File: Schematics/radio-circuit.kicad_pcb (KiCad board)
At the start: 4 copper layers, 59 x 29.5 mm, 36 parts, among them J2 STDC14, J3 0, J4 USB_A, U1 USBLC6-2SC6, U2 LD39015M33R, U3 STM32F042F6Px, U4 Si4705-D60-GM, Y1 SG-3030CM

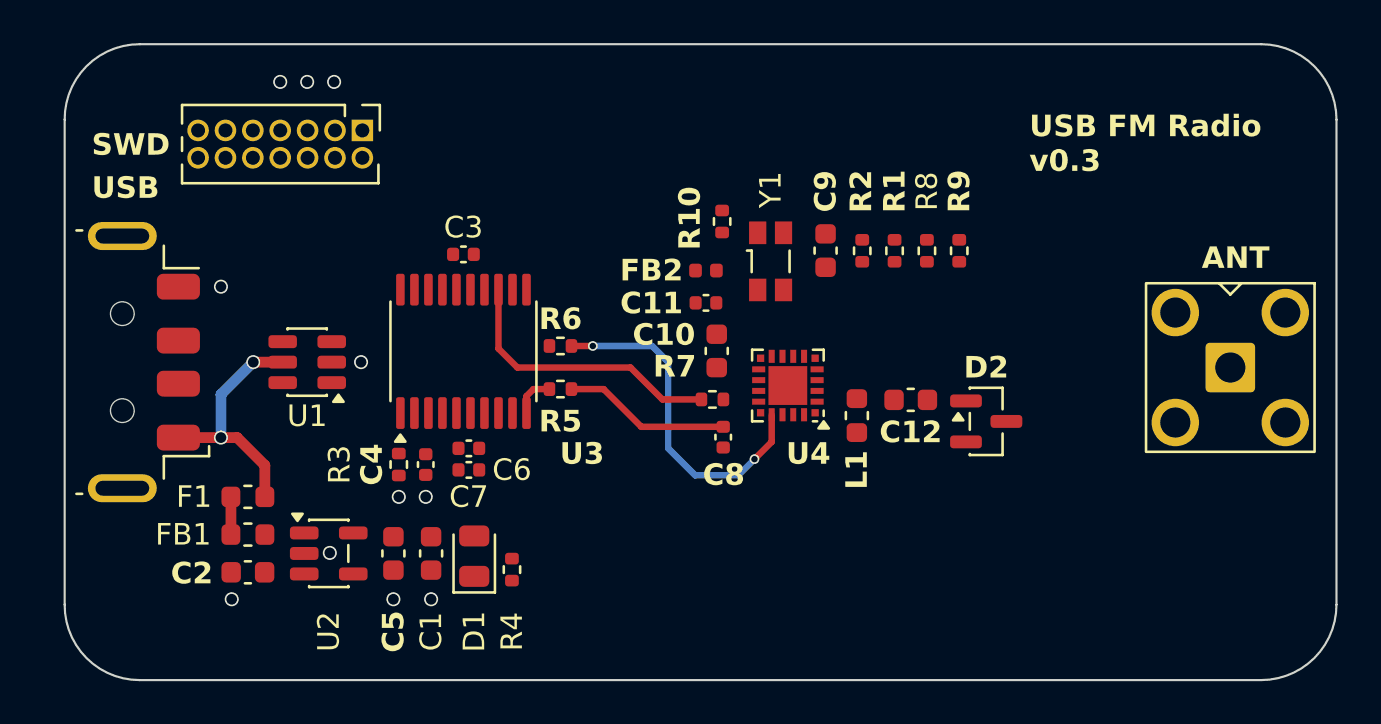
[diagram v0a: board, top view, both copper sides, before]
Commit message: Finished component placement
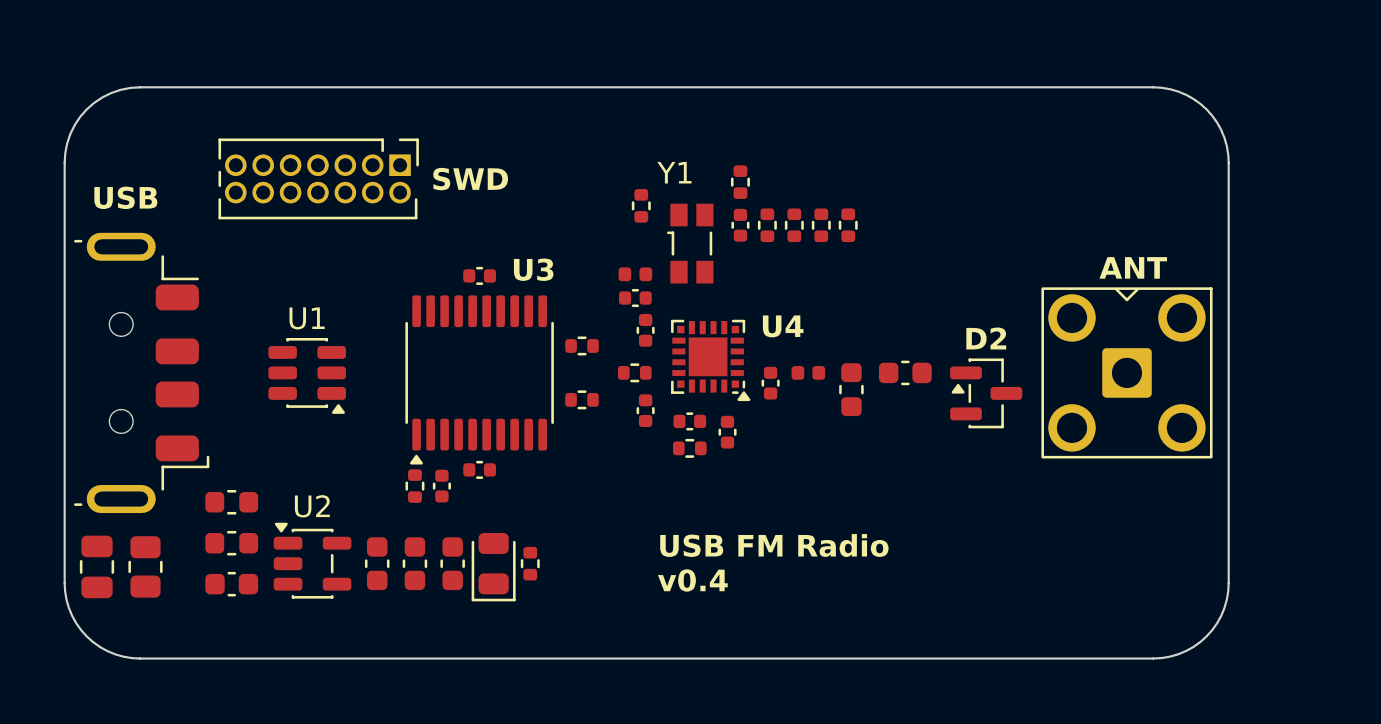
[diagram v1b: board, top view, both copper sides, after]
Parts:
- removed J4: USB_A, Local:USB_A_Molex_48037-2200_Horizontal
- added C13: 33p, Capacitor_SMD:C_0402_1005Metric, F.Cu at (192.8, 128.0)
- added C14: 6p, Capacitor_SMD:C_0402_1005Metric, F.Cu at (194.8, 125.7)
- added C15: 33p, Capacitor_SMD:C_0402_1005Metric, F.Cu at (191.0, 127.5)
- added C16: 1n, Capacitor_SMD:C_0603_1608Metric, F.Cu at (201.0, 125.2)
- added FB3: 75@100MHz, Inductor_SMD:L_0402_1005Metric, F.Cu at (196.5, 125.2)
- added J1: USB_A, Local:USB_A_Molex_48037-2200_Horizontal, F.Cu at (156.2, 125.2)
- added R11: 22, Resistor_SMD:R_0402_1005Metric, F.Cu at (193.3, 116.4)
- added R12: 10k, Resistor_SMD:R_0402_1005Metric, F.Cu at (188.8, 117.5)
- added R13: 330, Resistor_SMD:R_0402_1005Metric, F.Cu at (191.0, 128.8)
- C1: value 4.7u -> 100n; footprint Capacitor_SMD:C_0603_1608Metric -> Capacitor_SMD:C_0805_2012Metric
- C10: value 22n -> 100n; footprint Capacitor_SMD:C_0603_1608Metric -> Capacitor_SMD:C_0402_1005Metric
- C11: value 100n -> 22n
- C12: value 1n -> 100n; footprint Capacitor_SMD:C_0603_1608Metric -> Capacitor_SMD:C_0402_1005Metric
- C3: value 100n -> 4.7u; footprint Capacitor_SMD:C_0402_1005Metric -> Capacitor_SMD:C_0603_1608Metric
- C5: value 4.7u -> 100n; footprint Capacitor_SMD:C_0603_1608Metric -> Capacitor_SMD:C_0402_1005Metric
- C6: value 10n -> 4.7u; footprint Capacitor_SMD:C_0402_1005Metric -> Capacitor_SMD:C_0603_1608Metric
- C7: value 1u -> 10n
- C8: value 2.2p -> 1u; footprint Capacitor_SMD:C_0402_1005Metric -> Capacitor_SMD:C_0603_1608Metric
- C9: value 47n -> 2.2p; footprint Capacitor_SMD:C_0603_1608Metric -> Capacitor_SMD:C_0402_1005Metric
- R1: value 4k7 -> 1M; footprint Resistor_SMD:R_0402_1005Metric -> Resistor_SMD:R_0805_2012Metric
- R3: value 10k -> 4k7
- R4: value 1k5 -> 10k
- R5: value 2k -> 1k5
- R7: value 604 -> 2k
- R8: value 10k -> 604
- moved R1 37.7 mm to (165.8, 134.2), turned to 90 degrees
- moved R3 21.4 mm to (195.8, 118.4)
- moved C3 18.7 mm to (169.8, 135.1), turned to 180 degrees
- moved C1 15.5 mm to (163.5, 134.2), turned to 90 degrees
- moved R8 14.7 mm to (188.4, 125.2), turned to 0 degrees
- moved C8 13.9 mm to (180.0, 134.1)
- moved C12 12.7 mm to (188.9, 123.3), turned to -90 degrees
- moved C9 11.2 mm to (188.9, 127.0)
- moved R5 8.22 mm to (183.6, 134.1), turned to 90 degrees
- moved C7 8.02 mm to (181.2, 120.8)
- moved C2 7.76 mm to (178.2, 134.1), turned to -90 degrees
- moved R7 6.54 mm to (186.0, 124.0)
- moved R9 6.51 mm to (197.1, 118.4)
- moved C6 6.08 mm to (176.5, 134.1), turned to -90 degrees
- moved R4 5.94 mm to (178.2, 130.5), turned to -90 degrees
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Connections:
- C1 pad 1: +3.3V -> GND
- C1 pad 2: GND -> /SHD
- C10 pad 1: V_{RADIO} -> V_{OSC}
- C12 pad 1: /ANT -> V_{RADIO}
- C12 pad 2: /FMI -> GND
- C2 pad 1: V_{FILT} -> +3.3V
- C3 pad 1: +3.3V -> V_{LDO}
- C4 pad 1: NRST -> +3.3V
- C5 pad 1: +3.3V -> NRST
- C8 pad 1: I2S_WS -> +3.3V
- C9 pad 1: +3.3V -> I2S_WS
- FB1 pad 2: V_{FILT} -> V_{LDO}
- L1 pad 2: /FMI -> /TUNE
- R1 pad 1: +3.3V -> GND
- R1 pad 2: I2C_SCL -> /SHD
- R10 pad 1: OSC_EN -> GND
- R10 pad 2: GND -> ~{RD_RST}
- R2 pad 2: I2C_SDA -> I2C_SCL
- R3 pad 1: /BOOT -> +3.3V
- R3 pad 2: GND -> I2C_SDA
- R4 pad 1: /PWR_LED_K -> /BOOT
- R5 pad 1: /PA4 -> /PWR_LED_K
- R5 pad 2: I2S_WS -> GND
- R6 pad 1: /PA5 -> /PA4
- R6 pad 2: I2S_CK -> I2S_WS
- R7 pad 1: I2S_SD -> /PA5
- R7 pad 2: /DOUT -> I2S_CK
- R8 pad 1: GND -> I2S_SD
- R8 pad 2: / ~{SEN} -> /DOUT
- R9 pad 2: ~{RD_RST} -> / ~{SEN}
- U2 pad 1: V_{FILT} -> V_{LDO}
- U2 pad 3: V_{FILT} -> V_{LDO}
- U4 pad 18: ~{RD_IRQ} -> /GPO2
- U4 pad 19: unconnected-(U4-GPO1-Pad19) -> /GPO1
- Y1 pad 4: +3.3V -> V_{OSC}
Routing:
- net I2S_CK: track 16.0 -> 0.00 mm, vias 2 -> 0
- net I2S_SD: track 13.1 -> 0.00 mm
- net V_{BUS}: track 11.5 -> 0.00 mm, vias 2 -> 0
- net I2S_WS: track 7.76 -> 0.00 mm
- net /PA4: track 2.00 -> 0.00 mm
- net /FUSE: track 1.75 -> 0.00 mm
- net GND: vias 10 -> 0
- net +3.3V: vias 1 -> 0
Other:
- board size 59 x 29.5 mm -> 54 x 26.5 mm
- board text added: "USB FM Radio v0.4"
- board text removed: "USB FM Radio v0.3"

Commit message: Finished traces and layers
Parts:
- moved C5 14.4 mm to (170.7, 119.1), turned to 180 degrees
- moved R3 1.35 mm to (194.5, 118.4)
- moved R2 1.10 mm to (195.7, 118.4)
- moved R11 0.76 mm to (194.0, 116.8), turned to 0 degrees
- moved C1 0.50 mm to (164.0, 134.2)
- moved R1 0.50 mm to (166.2, 134.2)
- moved C11 0.32 mm to (188.2, 122.0)
- moved C12 0.30 mm to (188.8, 123.5)
- moved FB2 0.26 mm to (188.2, 120.8)
- moved R10 0.25 mm to (198.1, 118.4)
- moved C9 0.20 mm to (188.8, 127.0)
- moved R9 0.20 mm to (196.9, 118.4)
- moved R8 0.20 mm to (188.2, 125.2)
- moved C4 0.16 mm to (181.4, 129.8)
- moved R12 0.11 mm to (188.7, 117.4)
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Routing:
- net +3.3V: track 0.00 -> 56.6 mm, vias 0 -> 10
- net GND: track 0.00 -> 45.1 mm, vias 0 -> 97
- net ~{RD_RST}: track 0.00 -> 27.1 mm, vias 0 -> 2
- net I2C_SDA: track 0.00 -> 25.0 mm, vias 0 -> 2
- net I2C_SCL: track 0.00 -> 24.3 mm, vias 0 -> 2
- net NRST: track 0.00 -> 17.3 mm, vias 0 -> 2
- net /SHD: track 0.00 -> 15.7 mm
- net V_{BUS}: track 0.00 -> 10.5 mm, vias 0 -> 2
- net OSC_EN: track 0.00 -> 9.77 mm
- net /ANT: track 0.00 -> 9.55 mm
- net ~{RD_IRQ}: track 0.00 -> 8.74 mm
- net USB_D-: track 0.00 -> 8.63 mm
- net USB_D+: track 0.00 -> 7.82 mm
- net / ~{SEN}: track 0.00 -> 7.20 mm
- net I2S_SD: track 0.00 -> 7.16 mm
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- added copper zone on F.Cu, net +3.3V
- added copper zone on F.Cu, net /SHD
- added copper zone on B.Cu, net GND
- added copper zone on F.Cu, net GND
- added copper zone on In1.Cu, net GND
- added copper zone on In2.Cu, net GND

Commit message: Fixed via placement for QFN and re-routed STM32 NRST
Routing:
- net NRST: track 17.3 -> 21.4 mm
- net GND: track 45.1 -> 46.3 mm, vias 97 -> 95
